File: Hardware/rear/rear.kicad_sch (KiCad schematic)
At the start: 18 parts, among them J101 Conn_02x10_Odd_Even, J102 USB_B, J103 ARJC07-111071A, U101 AT24CS32-SSHM, U102 WE-TVS-82400102, U103 MCP3021

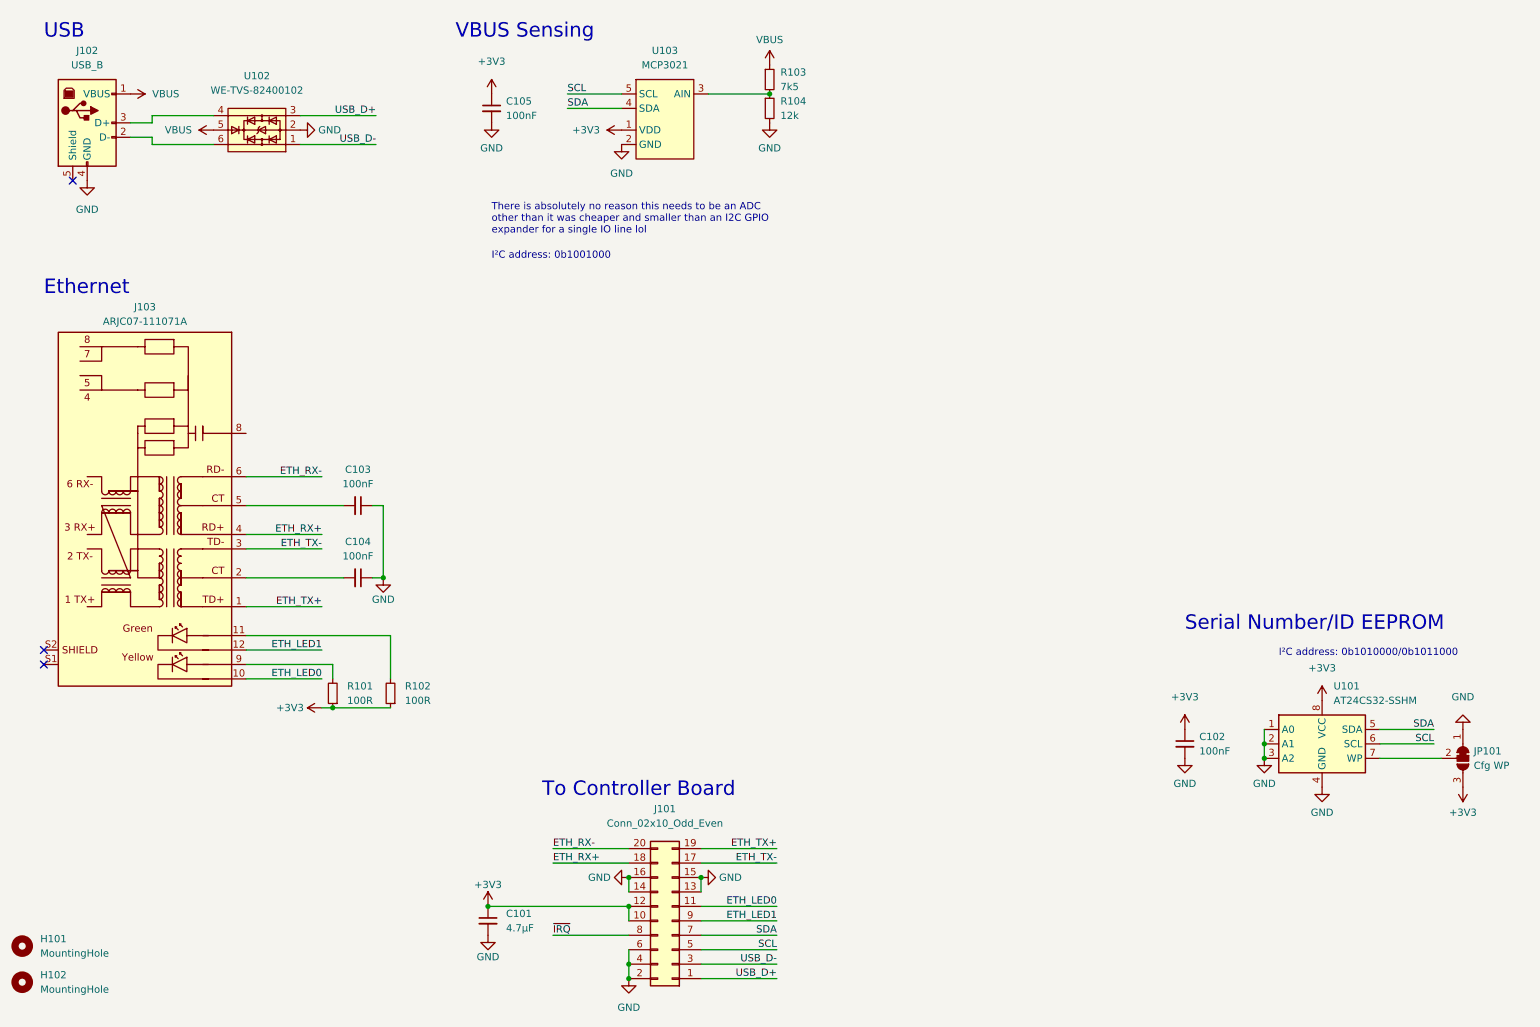
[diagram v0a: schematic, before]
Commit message: More new layout stuff
- More work on the new controller board layout

- Rework rear IO board for the new Technomet rear panel (it has an
  expansion connector for CAN also, and features four screw holes
  instead of two)

- Added a few footprints (expansion RJ45 connector; some
  horizontal/vertical headers)
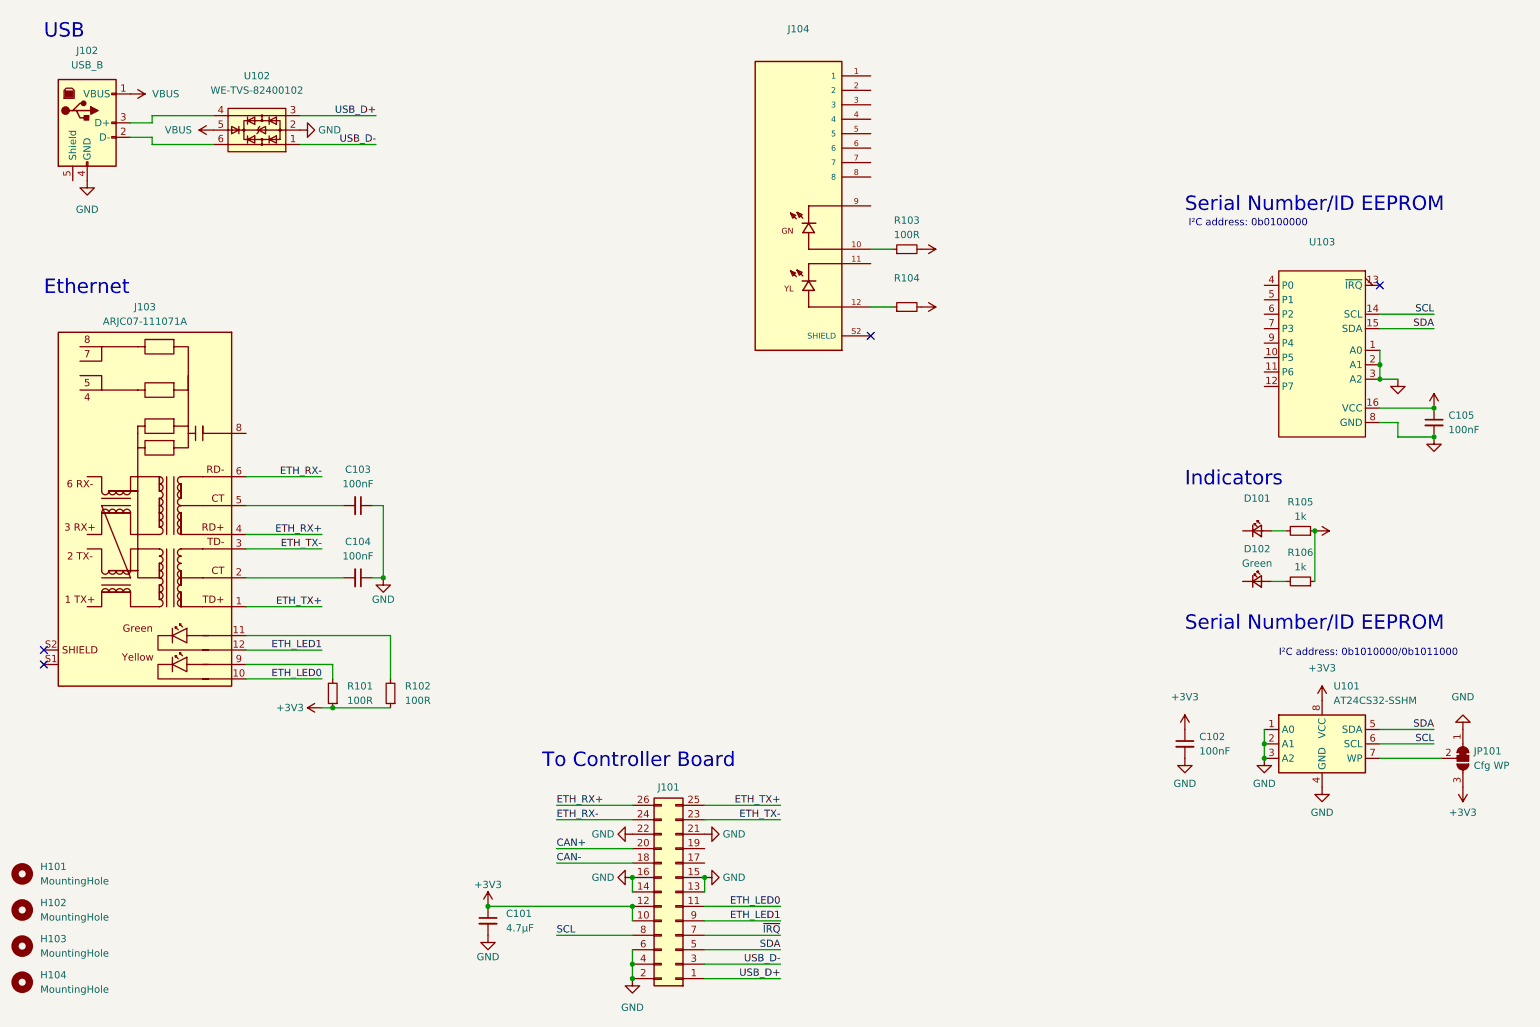
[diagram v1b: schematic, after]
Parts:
- removed J101: Conn_02x10_Odd_Even, Connector_PinHeader_1.27mm:PinHeader_2x10_P1.27mm_Vertical_SMD, symbol Connector_Generic:Conn_02x10_Odd_Even
- removed U103: MCP3021, Package_TO_SOT_SMD:SOT-23-5_HandSoldering, symbol programmable-load:MCP3021
- added D101: (no value), symbol Device:LED_Small
- added D102: Green, LED_SMD:LED_0805_2012Metric_Pad1.15x1.40mm_HandSolder, symbol Device:LED_Small
- added H103, H104: MountingHole, MountingHole:MountingHole_2.7mm_M2.5, symbol Mechanical:MountingHole
- added J101: Conn_02x10_Odd_Even, Connector_PinHeader_1.27mm:PinHeader_2x13_P1.27mm_Vertical, symbol Connector_Generic:Conn_02x13_Odd_Even
- added J104: (no value), programmable-load:CUI_CRJ061-L1-TH, symbol programmable-load:CRJ061-L1-TH
- added R105, R106: 1k, Resistor_SMD:R_0805_2012Metric_Pad1.20x1.40mm_HandSolder, symbol Device:R_Small
- added U103: (no value), symbol programmable-load:XRA1200
- R103: value 7k5 -> 100R; MPN WR08X752 JTL -> WR08X101 JTL
- R104: value 12k -> (none); footprint Resistor_SMD:R_0805_2012Metric_Pad1.20x1.40mm_HandSolder -> (none); MPN RMC1/10-123JTP -> WR08X101 JTL
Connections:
- net +3V3: now also R103.2, R104.2, J101.10 (Pin_10), J101.12 (Pin_12), R105.1, R106.1, U103.16 (VCC)
- net ETH_LED0: now also J101.11 (Pin_11)
- net ETH_LED1: now also J101.9 (Pin_9)
- net ETH_RX+: now also J101.26 (Pin_26)
- net ETH_RX-: now also J101.24 (Pin_24)
- net ETH_TX+: now also J101.25 (Pin_25)
- net ETH_TX-: now also J101.23 (Pin_23)
- net GND: now also J101.13 (Pin_13), J101.14 (Pin_14), J101.15 (Pin_15), J101.16 (Pin_16), J101.2 (Pin_2), J101.21 (Pin_21), J101.22 (Pin_22), J101.4 (Pin_4), J101.6 (Pin_6), U103.1 (A0), U103.2 (A1), U103.3 (A2), U103.8 (GND); no longer R104.2
- net SCL: now also J101.8 (Pin_8), U103.14 (SCL)
- net SDA: now also J101.5 (Pin_5), U103.15 (SDA)
- net USB_D+: now also J101.1 (Pin_1)
- net USB_D-: now also J101.3 (Pin_3)
- net VBUS: no longer R103.1
- net ~{IRQ}: now also J101.7 (Pin_7)
- net at R104.1: now also J104.12; no longer R103.2
- new net: D101.2 (A), R105.2
- new net: J104.10, R103.1
- new net: J104.S1 (SHIELD), J104.S2 (SHIELD)
- new net: D102.2 (A), R106.2
- new net CAN+: J101.20 (Pin_20)
- new net CAN-: J101.18 (Pin_18)
- no-connect marks 3 -> 4
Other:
- note added: "Indicators"
- note added: "I²C address: 0b0100000"
- note removed: "I²C address: 0b1001000"
- note removed: "There is absolutely no reason this needs to be an ADC other than it was cheaper and smaller than an I2C GPIO expander for a single IO line lol"
- note removed: "VBUS Sensing"
- moved on the sheet: H101, H102

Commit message: Rear IO rework
- Mostly finished the rear IO board rework (adding the CAN filtering and
  switchable termination; trigger input pulse shaper; fuses for
  expansion +12V)

- Changed encoder type on front panel for a shorter type

- Created schematic models and footprints for Bournds DR311 chokes;
  Mill-Max 2108 solder turrets
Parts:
- added C106: 100nF, Capacitor_SMD:C_0805_2012Metric_Pad1.18x1.45mm_HandSolder, symbol Device:C_Small
- added D103: ESDONCAN1, Package_TO_SOT_SMD:SOT-23_Handsoldering, symbol Device:D_TVS_Dual_AAC
- added D104: Panjit SS14, Diode_SMD:D_SMA_Handsoldering, symbol Device:D_Schottky_Small
- added D105: 1N4148W, Diode_SMD:D_SOD-123, symbol Diode:1N4148W
- added F101: 500mA, Fuse:Fuse_1206_3216Metric_Pad1.42x1.75mm_HandSolder, symbol Device:Polyfuse_Small
- added FB101: FerriteBead_Small, Inductor_SMD:L_0805_2012Metric_Pad1.05x1.20mm_HandSolder, symbol Device:FerriteBead_Small
- added J105: (no value), symbol Connector_Generic:Conn_01x01
- added J106: Conn_01x01, programmable-load:MillMax-2108-2, symbol Connector_Generic:Conn_01x01
- added L101: DR331-513BE, programmable-load:Bourns-DR331-0-0-MFG, symbol Device:L_Ferrite_Coupled_1423
- added R107: 1k, Resistor_SMD:R_0805_2012Metric_Pad1.20x1.40mm_HandSolder, symbol Device:R_Small
- added R108, R109: (no value), symbol Device:R_Small
- added R110: 47k, Resistor_SMD:R_0805_2012Metric_Pad1.20x1.40mm_HandSolder, symbol Device:R_Small
- added RV101: 500k, programmable-load:Potentiometer_Nidec_Copal_CT94EW, symbol Device:R_Potentiometer_Trim
- added TP101: Trigger, TestPoint:TestPoint_Keystone_5000-5004_Miniature, symbol Connector:TestPoint
- added U104: (no value), symbol programmable-load:TLP170A
- added U105: FODM217B, Package_SO:SOP-4_4.4x2.6mm_P1.27mm, symbol Isolator:FODM217B
- added U106: 74LVC1G17, Package_TO_SOT_SMD:SOT-23-5_HandSoldering, symbol 74xGxx:74LVC1G17
- C102: value 100nF -> (none); footprint Capacitor_SMD:C_0805_2012Metric_Pad1.18x1.45mm_HandSolder -> (none); MPN CL21B104KACNFNC -> CL21B105KBFNNNG
- D101: value (none) -> Green; footprint (none) -> LED_SMD:LED_0805_2012Metric_Pad1.15x1.40mm_HandSolder
- J104: value (none) -> CRJ061-L1-TH
- R104: value (none) -> 100R; footprint (none) -> Resistor_SMD:R_0805_2012Metric_Pad1.20x1.40mm_HandSolder
- U103: value (none) -> XRA1200; footprint (none) -> Package_SO:TSSOP-16_4.4x5mm_P0.65mm
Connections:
- net +3V3: now also C106.1, U105.4, U106.5 (VCC); no longer C102.1
- net GND: now also J101.17 (Pin_17), J104.7, J104.8, C106.2, D103.3 (common), R110.1, RV101.1, RV101.2, U104.3, U106.3 (GND); no longer C102.2, J101.15 (Pin_15), J101.16 (Pin_16)
- net ~{IRQ}: now also U103.13 (~{IRQ})
- net TRIGGER: now reaches J101.19 (Pin_19)
- net TRIGGER: now also U106.4
- net at J104.1: now also D103.2 (A2), L101.2
- net ~{EXT_LED1}: now reaches J104.11
- net ~{EXT_LED1}: now also U103.6 (P2)
- net at J104.2: now also D103.1 (A1), L101.1
- net at J104.4: now also J104.5, FB101.1
- net ~{EXT_LED0}: now reaches J104.9
- net ~{EXT_LED0}: now also U103.7 (P3)
- net at J104.S1 (SHIELD): no longer J104.S2 (SHIELD)
- net ~{LED_VSENSE}: now reaches D101.1 (K)
- net ~{LED_VSENSE}: now also U103.5 (P1)
- net ~{LED_TRIGGER}: now reaches D102.1 (K)
- net ~{LED_TRIGGER}: now also U103.4 (P0)
- net TERM_EN: now reaches U103.12 (P7)
- net TERM_EN: now also R107.2
- net CAN+ renamed CANH
- net CANH: now also L101.3, R108.2
- net CAN- renamed CANL
- net CANL: now also L101.4, U104.4
- new net: R108.1, U104.6
- new net: D105.1 (K), R109.1, U105.1
- new net: D105.2 (A), J106.1 (Pin_1), U105.2
- new net: C102.1, RV101.3, TP101.1, U106.2
- new net: J105.1 (Pin_1), R109.2
- new net: F101.1, FB101.2
- new net: D104.1 (K), F101.2
- new net: R107.1, U104.1
- new net: C102.2, R110.2, U105.3
- new net +12V: D104.2 (A), J101.15 (Pin_15), J101.16 (Pin_16)
- no-connect marks 4 -> 10
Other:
- note added: "CAN Termination"
- note added: "Expansion"
- note added: "External Trigger"
- note added: "IO Expander"
- title: Rear IO (USB + Ethernet) -> Rear IO
- moved on the sheet: C101, J101, R103, R104
